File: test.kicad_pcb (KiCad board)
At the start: 2 copper layers, 37 x 18 mm, 17 parts, among them Q1 MMBT7002K

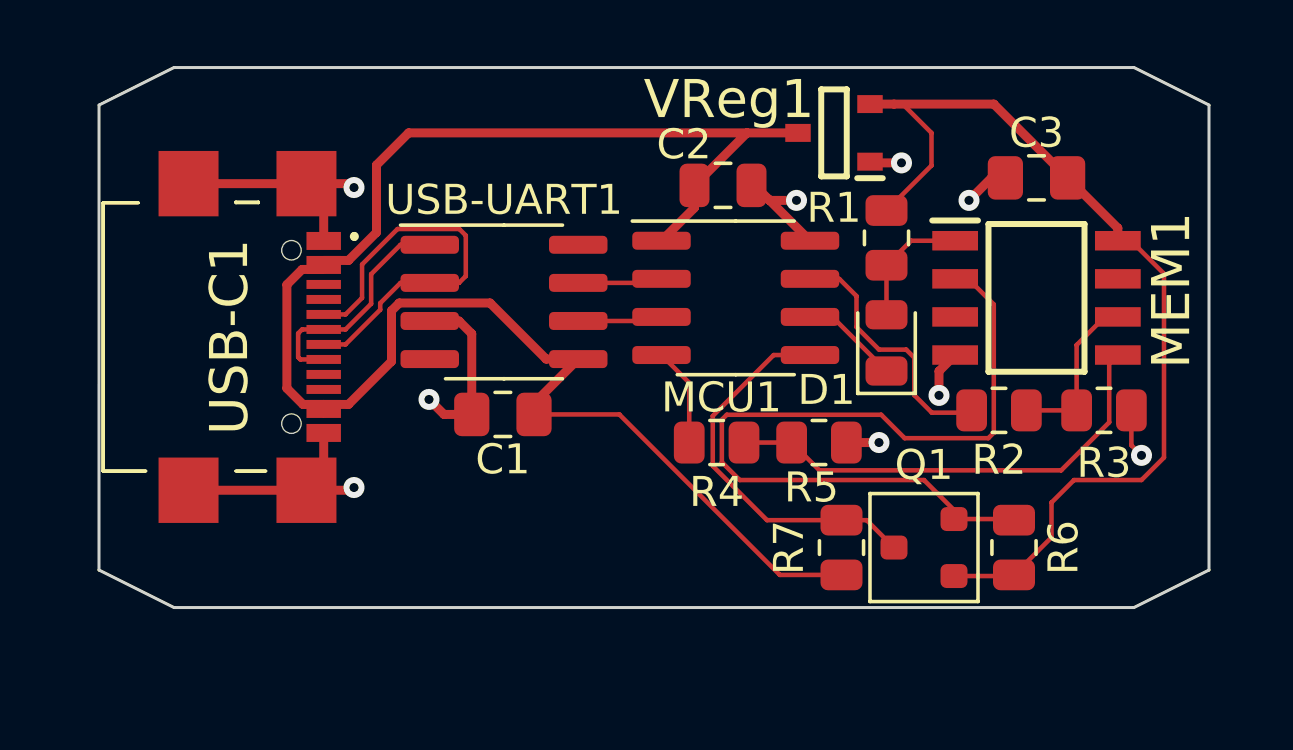
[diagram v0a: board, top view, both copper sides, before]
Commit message: Rerouted with bigger traces, default usb receptacle symbol
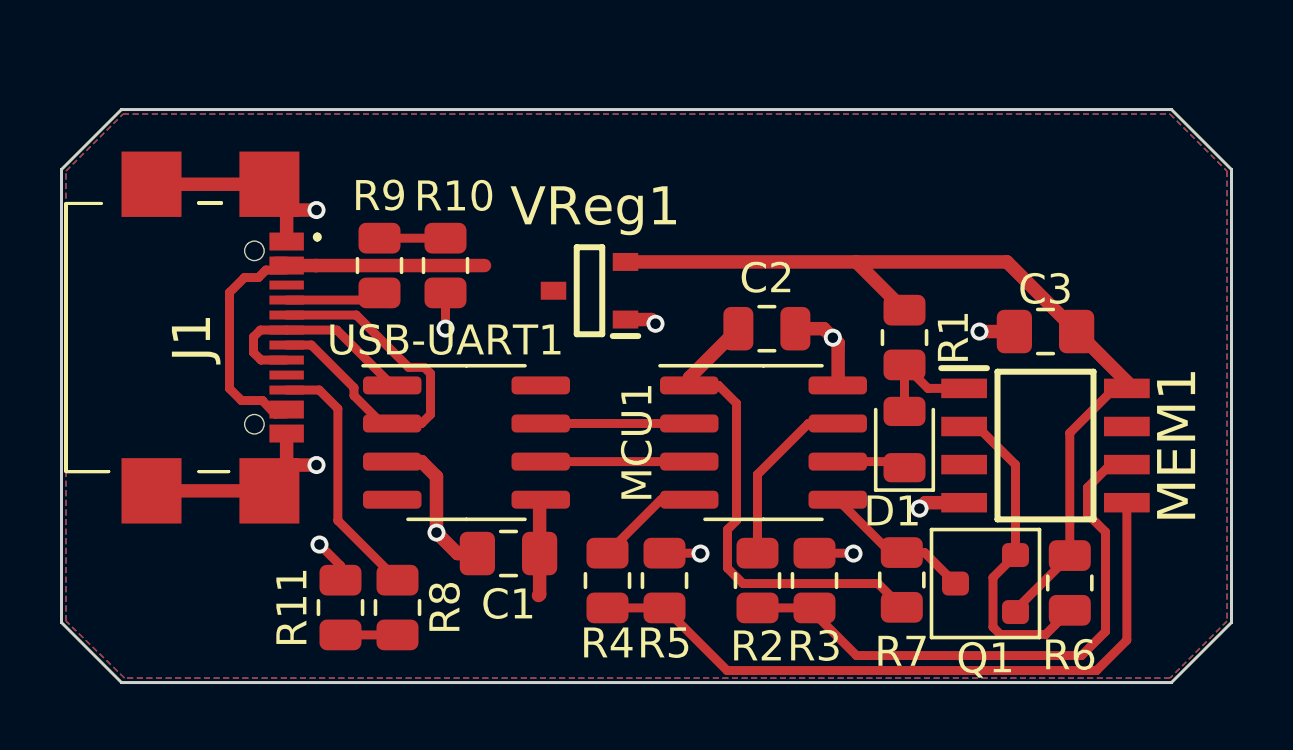
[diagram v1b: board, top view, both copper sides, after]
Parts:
- removed USB-C1: USB4110-GF-A, Samacsys:USB4110GFA
- added J1: USB_C_Receptacle_USB2.0, Samacsys:USB4110GFA_S, F.Cu at (113.8, 94.0)
- added R10: 3.9k, Resistor_SMD:R_0805_2012Metric, F.Cu at (122.8, 91.6)
- added R11: 3.9k, Resistor_SMD:R_0805_2012Metric, F.Cu at (119.3, 103.0)
- added R8: 1.2k, Resistor_SMD:R_0805_2012Metric, F.Cu at (121.2, 103.0)
- added R9: 1.2k, Resistor_SMD:R_0805_2012Metric, F.Cu at (120.6, 91.6)
- moved R3 11.2 mm to (135.1, 102.1), turned to 90 degrees
- moved R2 9.85 mm to (133.2, 102.1), turned to 90 degrees
- moved VReg1 9.70 mm to (127.6, 92.4)
- moved R5 6.91 mm to (130.1, 102.1), turned to 90 degrees
- moved R4 5.86 mm to (128.2, 102.1), turned to 90 degrees
- moved C3 5.13 mm to (142.8, 93.8)
- moved C2 5.00 mm to (133.5, 93.7)
- moved MEM1 4.93 mm to (142.8, 97.6)
- moved MCU1 4.91 mm to (133.4, 97.5)
- moved USB-UART1 4.85 mm to (123.5, 97.5)
- moved C1 4.64 mm to (124.9, 101.2)
- moved R1 3.38 mm to (138.1, 94.0)
- moved D1 3.28 mm to (138.1, 97.4)
- moved Q1 2.38 mm to (140.8, 102.2)
- moved R7 2.28 mm to (138.0, 102.1)
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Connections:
- net Earth renamed GND
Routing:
- net +5V: track 56.9 -> 33.6 mm
- net Net-(MEM1-SO(IO1)): track 27.6 -> 11.0 mm
- net Net-(MEM1-SCK): track 5.62 -> 19.4 mm
- net Net-(J1-CC2): track 0.00 -> 8.51 mm
- net PA2: track 12.9 -> 5.08 mm
- net Net-(MEM1-SI(IO0)): track 15.6 -> 23.2 mm
- net Net-(J1-CC1): track 0.00 -> 3.69 mm
- net PA3: track 8.60 -> 6.00 mm
- net +3.3V: track 32.7 -> 30.3 mm
- net Net-(R10-Pad2): track 0.00 -> 2.20 mm
- net Net-(MCU1-PA7): track 2.83 -> 4.95 mm
- net Net-(MCU1-PA6): track 2.83 -> 4.95 mm
- net Net-(R11-Pad2): track 0.00 -> 1.90 mm
- net PA0: track 3.30 -> 2.31 mm
- net GND: track 32.1 -> 33.0 mm, vias 9 -> 11
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- added copper zone on F.Cu, net +5V
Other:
- board size 37 x 18 mm -> 39 x 19.1 mm

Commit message: Programming pins
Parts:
- added J2: Conn_01x03, Connector_PinHeader_2.54mm:PinHeader_1x03_P2.54mm_Vertical, F.Cu at (132.7, 88.7)
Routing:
- net PA0: track 2.31 -> 29.9 mm
- net GND: track 33.0 -> 34.7 mm, vias 11 -> 12
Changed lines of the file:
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@@
+    )
+  )
+  (footprint "Connector_PinHeader_2.54mm:PinHeader_1x03_P2.54mm_Vertical" (layer "F.Cu")
+    (at 132.67 88.65 90)
+    (descr "Through hole straight pin header, 1x03, 2.54mm pitch, single row")
+    (tags "Through hole pin header THT 1x03 2.54mm single row")
+    (property "Sheetfile" "test.kicad_sch")
+    (property "Sheetname" "")
+    (property "ki_description" "Generic connector, single row, 01x03, script generated (kicad-library-utils/schlib/autogen/connector/)")
+    (property "ki_keywords" "connector")
+    (attr through_hole)
+    (fp_text reference "J2" (at 0.65 -2.37 90) (layer "F.SilkS")
+        (effects (font (size 1 1) (thickness 0.15)))
+    )
+    (fp_text value "Conn_01x03" (at 0 7.41 90) (layer "F.Fab")
+        (effects (font (size 1 1) (thickness 0.15)))
+    )
+    (fp_text user "${REFERENCE}" (at 0 2.54) (layer "F.Fab")
+        (effects (font (size 1 1) (thickness 0.15)))
+    )
+    (fp_line (start -1.33 -1.33) (end 0 -1.33)
+      (stroke (width 0.12) (type solid)) (layer "F.SilkS"))
+    (fp_line (start -1.33 0) (end -1.33 -1.33)
+      (stroke (width 0.12) (type solid)) (layer "F.SilkS"))
+    (fp_line (start -1.33 1.27) (end -1.33 6.41)
+      (stroke (width 0.12) (type solid)) (layer "F.SilkS"))
+    (fp_line (start -1.33 1.27) (end 1.33 1.27)
+      (stroke (width 0.12) (type solid)) (layer "F.SilkS"))
+    (fp_line (start -1.33 6.41) (end 1.33 6.41)
+      (stroke (width 0.12) (type solid)) (layer "F.SilkS"))
+    (fp_line (start 1.33 1.27) (end 1.33 6.41)
+      (stroke (width 0.12) (type solid)) (layer "F.SilkS"))
+    (fp_line (start -1.8 -1.8) (end -1.8 6.85)
+      (stroke (width 0.05) (type solid)) (layer "F.CrtYd"))
+    (fp_line (start -1.8 6.85) (end 1.8 6.85)
+      (stroke (width 0.05) (type solid)) (layer "F.CrtYd"))
+    (fp_line (start 1.8 -1.8) (end -1.8 -1.8)
+      (stroke (width 0.05) (type solid)) (layer "F.CrtYd"))
+    (fp_line (start 1.8 6.85) (end 1.8 -1.8)
+      (stroke (width 0.05) (type solid)) (layer "F.CrtYd"))
+    (fp_line (start -1.27 -0.635) (end -0.635 -1.27)
+      (stroke (width 0.1) (type solid)) (layer "F.Fab"))
+    (fp_line (start -1.27 6.35) (end -1.27 -0.635)
+      (stroke (width 0.1) (type solid)) (layer "F.Fab"))
+    (fp_line (start -0.635 -1.27) (end 1.27 -1.27)
+      (stroke (width 0.1) (type solid)) (layer "F.Fab"))
+    (fp_line (start 1.27 -1.27) (end 1.27 6.35)
+      (stroke (width 0.1) (type solid)) (layer "F.Fab"))
+    (fp_line (start 1.27 6.35) (end -1.27 6.35)
+      (stroke (width 0.1) (type solid)) (layer "F.Fab"))
+    (pad "1" thru_hole rect (at 0 0 90) (size 1.7 1.7) (drill 1) (layers "*.Cu" "*.Mask")
+      (net 1 "+5V") (pinfunction "Pin_1") (pintype "passive"))
+    (pad "2" thru_hole oval (at 0 2.54 90) (size 1.7 1.7) (drill 1) (layers "*.Cu" "*.Mask")
+      (net 2 "GND") (pinfunction "Pin_2") (pintype "passive"))
+    (pad "3" thru_hole oval (at 0 5.08 90) (size 1.7 1.7) (drill 1) (layers "*.Cu" "*.Mask")
+      (net 3 "PA0") (pinfunction "Pin_3") (pintype "passive"))
+    (model "${KICAD6_3DMODEL_DIR}/Connector_PinHeader_2.54mm.3dshapes/PinHeader_1x03_P2.54mm_Vertical.wrl"
+      (offset (xyz 0 0 0))
+      (scale (xyz 1 1 1))
+      (rotate (xyz 0 0 0))
     )
   )
@@
   (segment (start 117.79 89.75) (end 118.5 89.75) (width 0.45) (layer "F.Cu") (net 2))
   (segment (start 135.1 101.1875) (end 136.3875 101.1875) (width 0.3) (layer "F.Cu") (net 2))
+  (segment (start 134.3 90) (end 134.3 89.56) (width 0.45) (layer "F.Cu") (net 2))
   (segment (start 122.5 98.635001) (end 121.999999 98.135) (width 0.45) (layer "F.Cu") (net 2))
   (segment (start 135.887 95.5) (end 135.887 94.18) (width 0.45) (layer "F.Cu") (net 2))
@@
   (segment (start 135.712 94.005) (end 135.412 93.705) (width 0.45) (layer "F.Cu") (net 2))
   (segment (start 136.3875 101.1875) (end 136.4 101.2) (width 0.3) (layer "F.Cu") (net 2))
+  (segment (start 134.3 89.56) (end 135.21 88.65) (width 0.45) (layer "F.Cu") (net 2))
   (segment (start 119.3 102.0875) (end 119.3 101.6) (width 0.3) (layer "F.Cu") (net 2))
   (via (at 118.5 89.75) (size 0.6) (drill 0.35) (layers "F.Cu" "B.Cu") (net 2))
@@
   (via (at 140.6 93.8) (size 0.6) (drill 0.35) (layers "F.Cu" "B.Cu") (net 2))
   (via (at 136.4 101.2) (size 0.6) (drill 0.35) (layers "F.Cu" "B.Cu") (net 2))
+  (via (at 134.3 90) (size 0.6) (drill 0.35) (layers "F.Cu" "B.Cu") (free) (net 2))
   (via (at 118.6 100.9) (size 0.6) (drill 0.35) (layers "F.Cu" "B.Cu") (free) (net 2))
   (via (at 135.712 94.005) (size 0.6) (drill 0.35) (layers "F.Cu" "B.Cu") (net 2))
@@
   (via (at 122.5 100.5) (size 0.6) (drill 0.35) (layers "F.Cu" "B.Cu") (free) (net 2))
   (via (at 122.8 93.7) (size 0.6) (drill 0.35) (layers "F.Cu" "B.Cu") (net 2))
+  (segment (start 136.849999 98.135) (end 135.875 98.135) (width 0.25) (layer "F.Cu") (net 3))
+  (segment (start 135.6 92.4) (end 137.125 93.925) (width 0.25) (layer "F.Cu") (net 3))
+  (segment (start 127.7 91.2) (end 127.7 92) (width 0.25) (layer "F.Cu") (net 3))
+  (segment (start 127.7 92) (end 128.1 92.4) (width 0.25) (layer "F.Cu") (net 3))
+  (segment (start 128.1 92.4) (end 135.6 92.4) (width 0.25) (layer "F.Cu") (net 3))
+  (segment (start 136 90.6) (end 128.3 90.6) (width 0.25) (layer "F.Cu") (net 3))
+  (segment (start 137.125 97.859999) (end 136.849999 98.135) (width 0.25) (layer "F.Cu") (net 3))
+  (segment (start 128.3 90.6) (end 127.7 91.2) (width 0.25) (layer "F.Cu") (net 3))
+  (segment (start 137.75 88.65) (end 137.75 88.85) (width 0.25) (layer "F.Cu") (net 3))
   (segment (start 135.875 98.135) (end 137.8975 98.135) (width 0.3) (layer "F.Cu") (net 3))
   (segment (start 137.8975 98.135) (end 138.1 98.3375) (width 0.3) (layer "F.Cu") (net 3))
+  (segment (start 137.125 93.925) (end 137.125 97.859999) (width 0.25) (layer "F.Cu") (net 3))
+  (segment (start 137.75 88.85) (end 136 90.6) (width 0.25) (layer "F.Cu") (net 3))
   (segment (start 138.1 94.9125) (end 138.1 96.4625) (width 0.3) (layer "F.Cu") (net 4))
   (segment (start 140.088 95.695) (end 138.8825 95.695) (width 0.3) (layer "F.Cu") (net 4))
